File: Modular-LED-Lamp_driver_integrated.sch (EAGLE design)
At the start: 15 parts

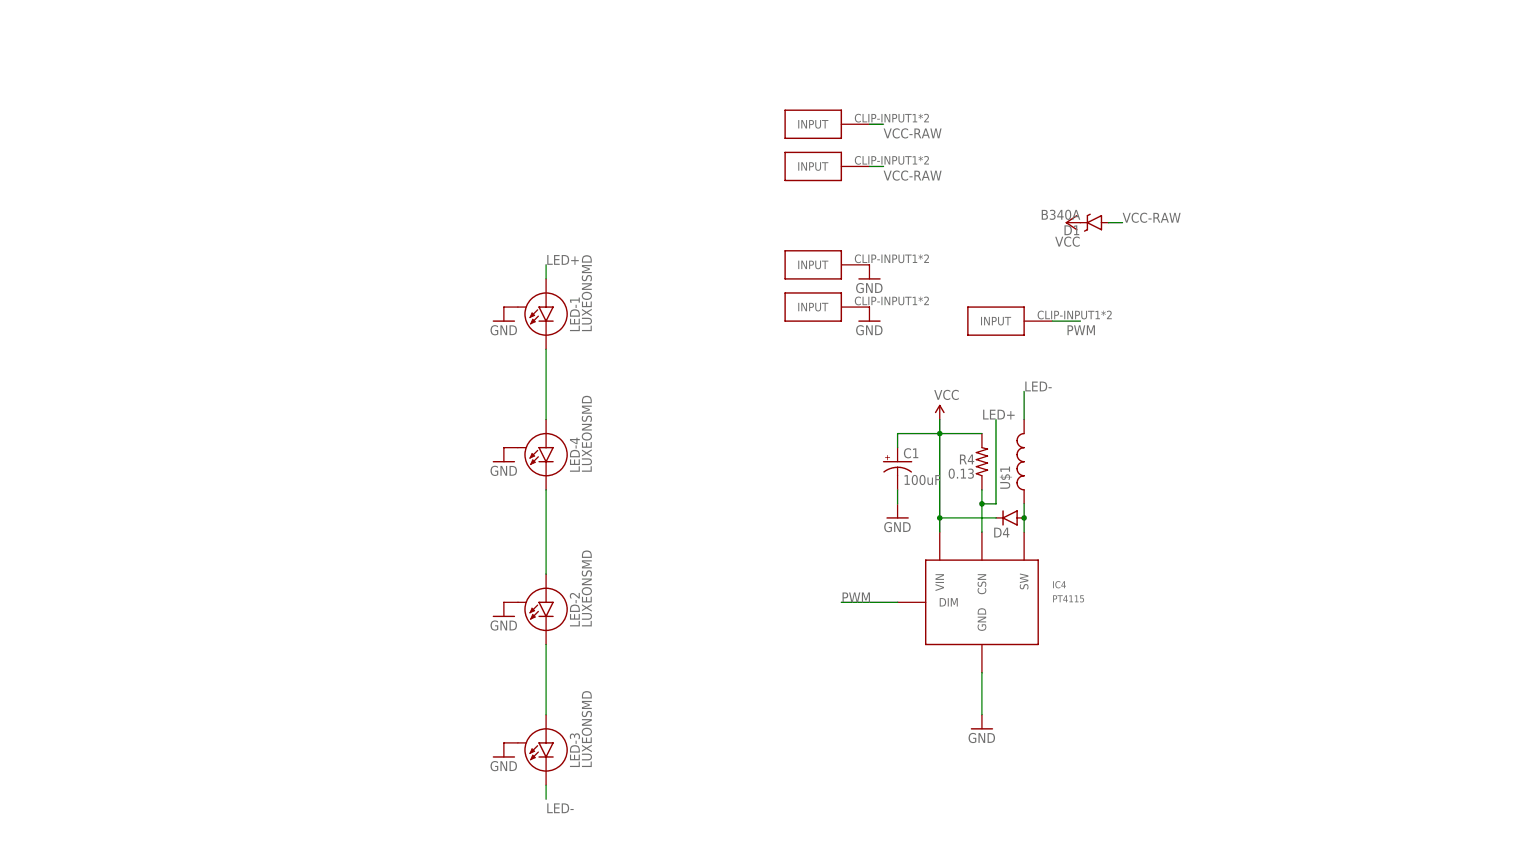
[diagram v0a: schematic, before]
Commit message: changed outline to be bigger to disspate more heat, added footprint for 90° turned fuse holders, rounded edges
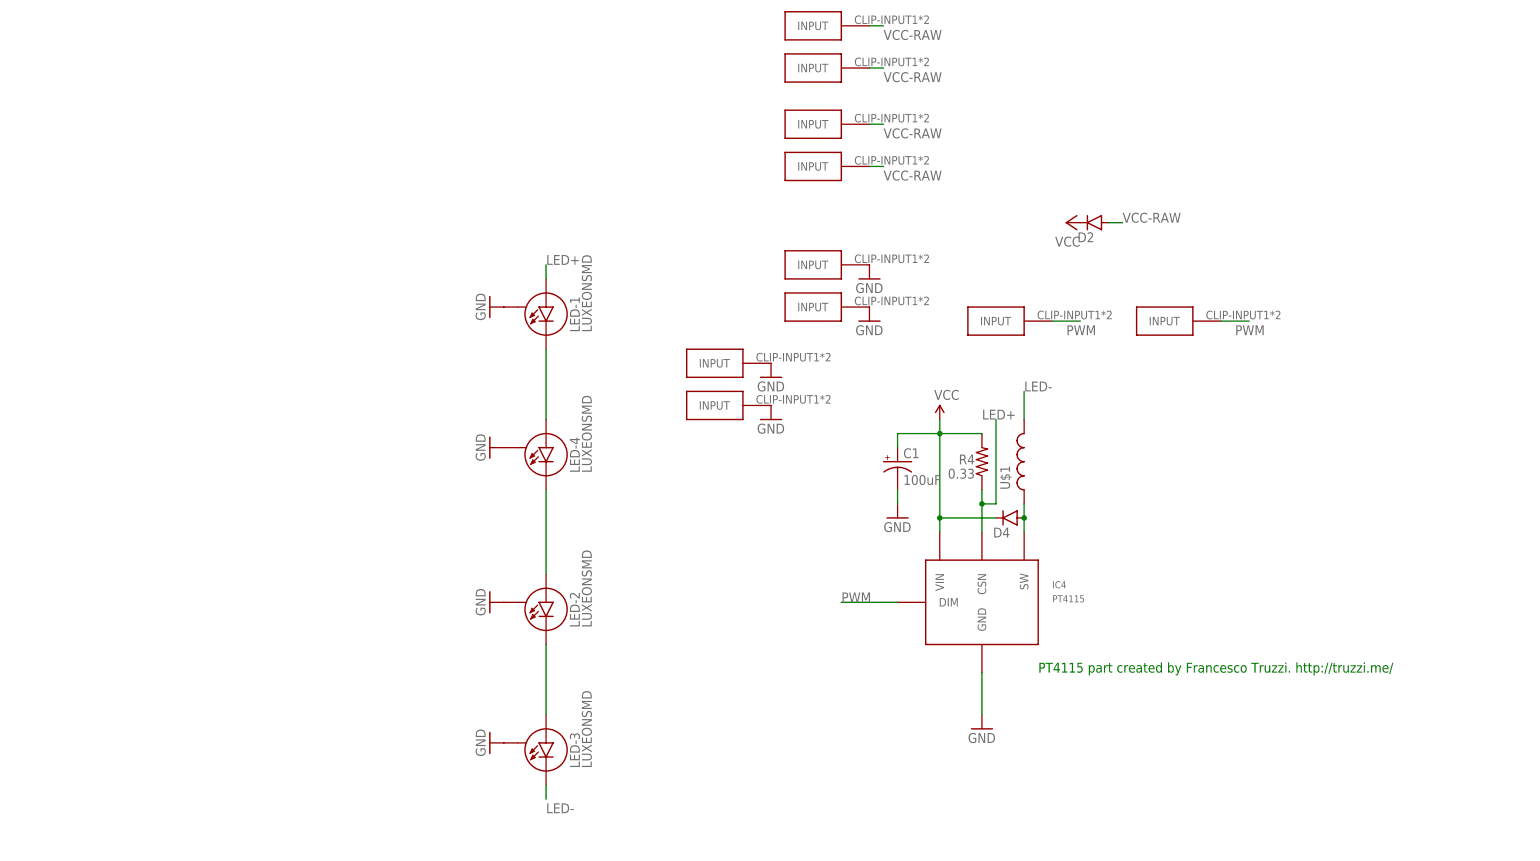
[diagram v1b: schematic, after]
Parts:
- removed D1: B340A, SparkFun-DiscreteSemi:DIODE-SCHOTTKY-B340A
- added D2: (no value), SparkFun-DiscreteSemi:DIODESMA-KIT
- added GND-CLIP1, GND-CLIP3: GND, timon-diverses:FUSE-HOLDER-5X20MM
- added PWM-CLIP1, VCC-CLIP1, VCC-CLIP3: FUSE-HOLDER-5X20MM, timon-diverses:FUSE-HOLDER-5X20MM
- R4: value 0.13 -> 0.33
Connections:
- net GND: now also GND-CLIP1.INPUT, GND-CLIP3.INPUT
- net PWM: now also PWM-CLIP1.INPUT
- net VCC: now also D2.C; no longer D1.C
- net VCC-RAW: now also D2.A, VCC-CLIP1.INPUT, VCC-CLIP3.INPUT; no longer D1.A
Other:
- note added: "PT4115 part created by Francesco Truzzi. http://truzzi.me/"
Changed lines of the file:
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@@
 <part name="SUPPLY4" library="SparkFun-Aesthetics" deviceset="VCC" device=""/>
 <part name="GND8" library="SparkFun-Aesthetics" deviceset="GND" device=""/>
-<part name="R4" library="SparkFun-Resistors" deviceset="0.3OHM-1/8W-1%(0805)" device="" value="0.13"/>
+<part name="R4" library="SparkFun-Resistors" deviceset="0.3OHM-1/8W-1%(0805)" device="" value="0.33"/>
 <part name="D4" library="SparkFun-DiscreteSemi" deviceset="DIODE" device="SMA-KIT"/>
 <part name="GND9" library="SparkFun-Aesthetics" deviceset="GND" device=""/>
 <part name="C1" library="SparkFun-Capacitors" deviceset="CAP_POL" device="E" value="100uF"/>
-<part name="D1" library="SparkFun-DiscreteSemi" deviceset="DIODE-SCHOTTKY" device="-B340A" value="B340A"/>
+<part name="U$1" library="inductor-coilcraft" deviceset="MSS1260" device=""/>
 <part name="GND1" library="supply1" deviceset="GND" device=""/>
 <part name="GND2" library="supply1" deviceset="GND" device=""/>
 <part name="GND3" library="supply1" deviceset="GND" device=""/>
 <part name="GND4" library="supply1" deviceset="GND" device=""/>
-<part name="U$1" library="inductor-coilcraft" deviceset="MSS1260" device=""/>
+<part name="VCC-CLIP1" library="timon-diverses" deviceset="FUSE-HOLDER-5X20MM" device=""/>
+<part name="VCC-CLIP3" library="timon-diverses" deviceset="FUSE-HOLDER-5X20MM" device=""/>
+<part name="GND-CLIP1" library="timon-diverses" deviceset="FUSE-HOLDER-5X20MM" device="" value="GND"/>
+<part name="GND-CLIP3" library="timon-diverses" deviceset="FUSE-HOLDER-5X20MM" device="" value="GND"/>
+<part name="GND5" library="supply1" deviceset="GND" device=""/>
+<part name="GND6" library="supply1" deviceset="GND" device=""/>
+<part name="PWM-CLIP1" library="timon-diverses" deviceset="FUSE-HOLDER-5X20MM" device=""/>
+<part name="D2" library="SparkFun-DiscreteSemi" deviceset="DIODE" device="SMA-KIT"/>
 </parts>
 <sheets>
 <sheet>
 <plain>
+<text x="111.76" y="-38.1" size="1.778" layer="91">PT4115 part created by Francesco Truzzi. http://truzzi.me/</text>
 </plain>
 <instances>
@@
 <instance part="GND9" gate="1" x="86.36" y="-10.16"/>
 <instance part="C1" gate="G$1" x="86.36" y="0"/>
-<instance part="D1" gate="G$1" x="121.92" y="43.18" rot="R180"/>
-<instance part="GND1" gate="1" x="15.24" y="-27.94"/>
-<instance part="GND2" gate="1" x="15.24" y="-53.34"/>
-<instance part="GND3" gate="1" x="15.24" y="0"/>
-<instance part="GND4" gate="1" x="15.24" y="25.4"/>
 <instance part="U$1" gate="G$1" x="109.22" y="0"/>
+<instance part="GND1" gate="1" x="12.7" y="27.94" rot="R270"/>
+<instance part="GND2" gate="1" x="12.7" y="2.54" rot="R270"/>
+<instance part="GND3" gate="1" x="12.7" y="-25.4" rot="R270"/>
+<instance part="GND4" gate="1" x="12.7" y="-50.8" rot="R270"/>
+<instance part="VCC-CLIP1" gate="CLIP" x="71.12" y="78.74"/>
+<instance part="VCC-CLIP3" gate="CLIP" x="71.12" y="71.12"/>
+<instance part="GND-CLIP1" gate="CLIP" x="53.34" y="17.78"/>
+<instance part="GND-CLIP3" gate="CLIP" x="53.34" y="10.16"/>
+<instance part="GND5" gate="1" x="63.5" y="15.24"/>
+<instance part="GND6" gate="1" x="63.5" y="7.62"/>
+<instance part="PWM-CLIP1" gate="CLIP" x="134.62" y="25.4"/>
+<instance part="D2" gate="G$1" x="121.92" y="43.18" smashed="yes" rot="R180">
+<attribute name="NAME" x="121.92" y="41.4274" size="1.778" layer="95" rot="R180"/>
+<attribute name="VALUE" x="119.38" y="45.4914" size="1.778" layer="96" rot="R180"/>
+</instance>
 </instances>
 <busses>
@@
 <segment>
 <pinref part="P+1" gate="VCC" pin="VCC"/>
-<pinref part="D1" gate="G$1" pin="C"/>
+<pinref part="D2" gate="G$1" pin="C"/>
 </segment>
 </net>
@@
 </segment>
 <segment>
+<pinref part="LED-1" gate="G$1" pin="S"/>
+<pinref part="GND1" gate="1" pin="GND"/>
+</segment>
+<segment>
+<pinref part="LED-4" gate="G$1" pin="S"/>
+<pinref part="GND2" gate="1" pin="GND"/>
+</segment>
+<segment>
 <pinref part="LED-2" gate="G$1" pin="S"/>
-<pinref part="GND1" gate="1" pin="GND"/>
-</segment>
-<segment>
-<pinref part="LED-4" gate="G$1" pin="S"/>
 <pinref part="GND3" gate="1" pin="GND"/>
 </segment>
 <segment>
-<pinref part="LED-1" gate="G$1" pin="S"/>
+<pinref part="LED-3" gate="G$1" pin="S"/>
 <pinref part="GND4" gate="1" pin="GND"/>
 </segment>
 <segment>
-<pinref part="LED-3" gate="G$1" pin="S"/>
-<pinref part="GND2" gate="1" pin="GND"/>
+<pinref part="GND-CLIP1" gate="CLIP" pin="INPUT"/>
+<pinref part="GND5" gate="1" pin="GND"/>
+</segment>
+<segment>
+<pinref part="GND-CLIP3" gate="CLIP" pin="INPUT"/>
+<pinref part="GND6" gate="1" pin="GND"/>
 </segment>
 </net>
@@
 <label x="76.2" y="-25.4" size="1.778" layer="95"/>
 </segment>
+<segment>
+<pinref part="PWM-CLIP1" gate="CLIP" pin="INPUT"/>
+<wire x1="144.78" y1="25.4" x2="149.86" y2="25.4" width="0.1524" layer="91"/>
+<label x="147.32" y="22.86" size="1.778" layer="95"/>
+</segment>
 </net>
 <net name="N$1" class="0">
@@
 <net name="VCC-RAW" class="0">
 <segment>
-<pinref part="D1" gate="G$1" pin="A"/>
 <wire x1="124.46" y1="43.18" x2="127" y2="43.18" width="0.1524" layer="91"/>
 <label x="127" y="43.18" size="1.778" layer="95"/>
+<pinref part="D2" gate="G$1" pin="A"/>
 </segment>
 <segment>
@@
 <pinref part="VCC-CLIP2" gate="CLIP" pin="INPUT"/>
 </segment>
-</net>
+<segment>
+<wire x1="81.28" y1="78.74" x2="83.82" y2="78.74" width="0.1524" layer="91"/>
+<label x="83.82" y="76.2" size="1.778" layer="95"/>
+<pinref part="VCC-CLIP1" gate="CLIP" pin="INPUT"/>
+</segment>
+<segment>
+<wire x1="81.28" y1="71.12" x2="83.82" y2="71.12" width="0.1524" layer="91"/>
+<label x="83.82" y="68.58" size="1.778" layer="95"/>
+<pinref part="VCC-CLIP3" gate="CLIP" pin="INPUT"/>
+</segment>
+</net>

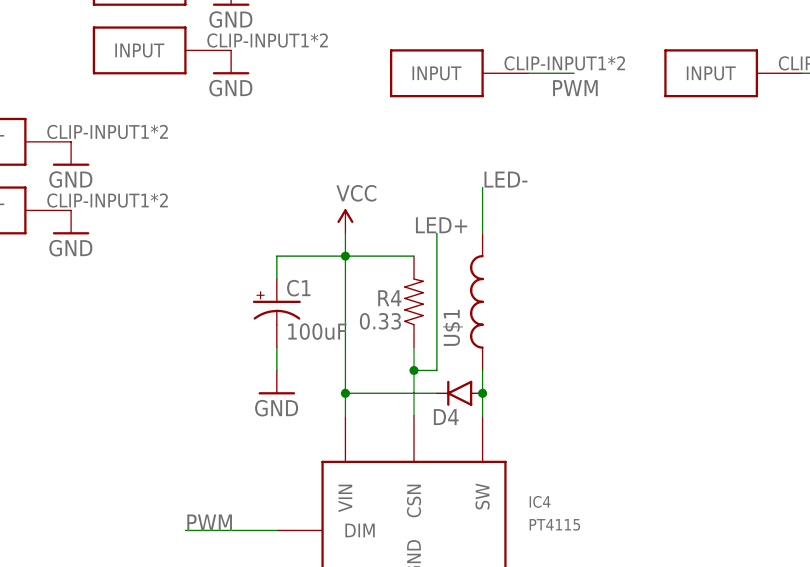
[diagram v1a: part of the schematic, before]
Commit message: updated integrated driver module to be 1W instead of 3W
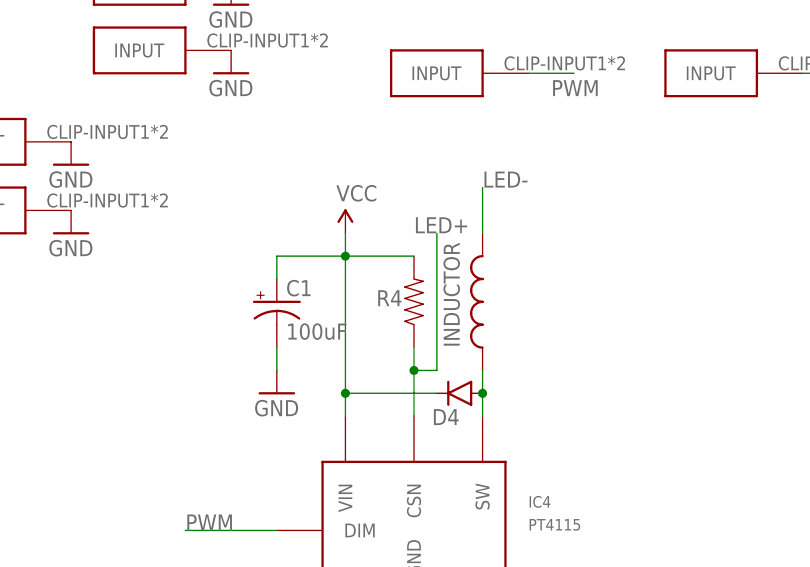
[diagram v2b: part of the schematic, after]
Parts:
- R4: value 0.33 -> 0.3; device SparkFun-Resistors:0.3OHM-1/8W-1%(0805) -> SparkFun-Resistors:RESISTOR1206
- renumbered U$1 to INDUCTOR
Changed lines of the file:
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@@
 <class number="0" name="default" width="0" drill="0">
+</class>
+<class number="1" name="VCC" width="0" drill="0">
+<clearance class="1" value="0.762"/>
 </class>
 </classes>
@@
 <part name="SUPPLY4" library="SparkFun-Aesthetics" deviceset="VCC" device=""/>
 <part name="GND8" library="SparkFun-Aesthetics" deviceset="GND" device=""/>
-<part name="R4" library="SparkFun-Resistors" deviceset="0.3OHM-1/8W-1%(0805)" device="" value="0.33"/>
+<part name="R4" library="SparkFun-Resistors" deviceset="RESISTOR" device="1206" value="0.3"/>
 <part name="D4" library="SparkFun-DiscreteSemi" deviceset="DIODE" device="SMA-KIT"/>
 <part name="GND9" library="SparkFun-Aesthetics" deviceset="GND" device=""/>
 <part name="C1" library="SparkFun-Capacitors" deviceset="CAP_POL" device="E" value="100uF"/>
-<part name="U$1" library="inductor-coilcraft" deviceset="MSS1260" device=""/>
+<part name="INDUCTOR" library="inductor-coilcraft" deviceset="MSS1260" device=""/>
 <part name="GND1" library="supply1" deviceset="GND" device=""/>
 <part name="GND2" library="supply1" deviceset="GND" device=""/>
@@
 <instance part="R4" gate="G$1" x="101.6" y="0" smashed="yes" rot="R90">
 <attribute name="NAME" x="100.33" y="1.2954" size="1.778" layer="95" rot="R180"/>
-<attribute name="VALUE" x="100.33" y="-1.27" size="1.778" layer="96" rot="R180"/>
 </instance>
 <instance part="D4" gate="G$1" x="106.68" y="-10.16" smashed="yes" rot="R180">
@@
 <instance part="GND9" gate="1" x="86.36" y="-10.16"/>
 <instance part="C1" gate="G$1" x="86.36" y="0"/>
-<instance part="U$1" gate="G$1" x="109.22" y="0"/>
+<instance part="INDUCTOR" gate="G$1" x="109.22" y="0"/>
 <instance part="GND1" gate="1" x="12.7" y="27.94" rot="R270"/>
 <instance part="GND2" gate="1" x="12.7" y="2.54" rot="R270"/>
@@
 <wire x1="109.22" y1="7.62" x2="109.22" y2="12.7" width="0.1524" layer="91"/>
 <label x="109.22" y="12.7" size="1.778" layer="95"/>
-<pinref part="U$1" gate="G$1" pin="P$1"/>
+<pinref part="INDUCTOR" gate="G$1" pin="P$1"/>
 </segment>
 </net>
@@
 <wire x1="109.22" y1="-7.62" x2="109.22" y2="-10.16" width="0.1524" layer="91"/>
 <junction x="109.22" y="-10.16"/>
-<pinref part="U$1" gate="G$1" pin="P$2"/>
-</segment>
-</net>
-<net name="VCC-RAW" class="0">
+<pinref part="INDUCTOR" gate="G$1" pin="P$2"/>
+</segment>
+</net>
+<net name="VCC-RAW" class="1">
 <segment>
 <wire x1="124.46" y1="43.18" x2="127" y2="43.18" width="0.1524" layer="91"/>

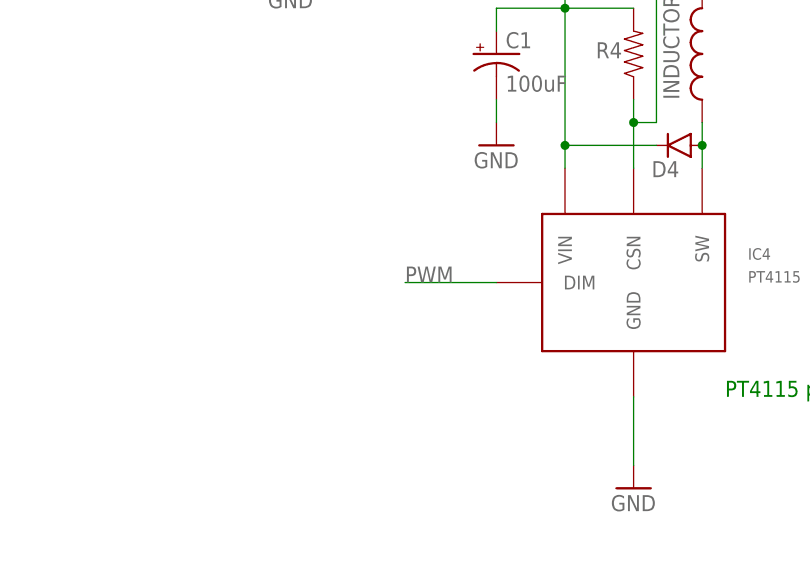
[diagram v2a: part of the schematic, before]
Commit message: fixed issued with PWM rod causing short circuit when two boards are mounted with one being reversed. Added PDF for schematic and board.
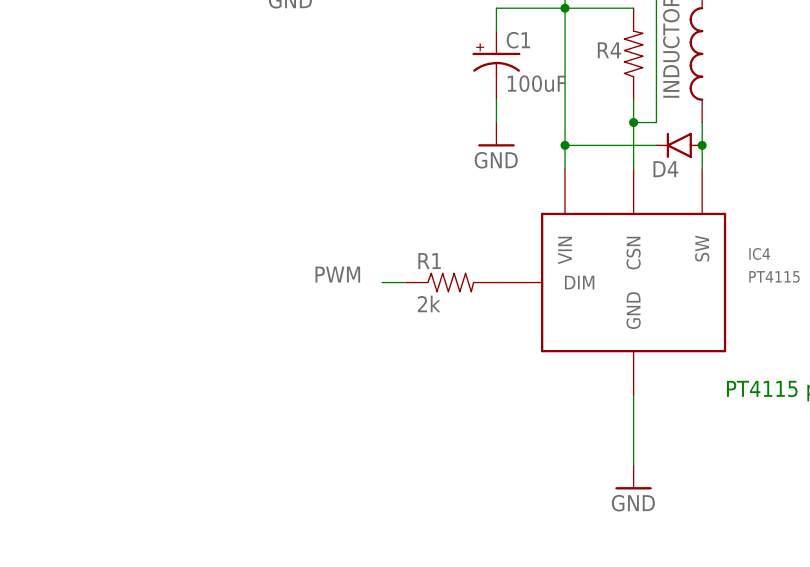
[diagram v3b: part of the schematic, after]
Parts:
- added R1: 2k, SparkFun-Resistors:RESISTOR1206
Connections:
- new net N$5: IC4.DIM, R1.2
- net PWM: now also R1.1; no longer IC4.DIM
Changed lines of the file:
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@@
 <part name="PWM-CLIP1" library="timon-diverses" deviceset="FUSE-HOLDER-5X20MM" device=""/>
 <part name="D2" library="SparkFun-DiscreteSemi" deviceset="DIODE" device="SMA-KIT"/>
+<part name="R1" library="SparkFun-Resistors" deviceset="RESISTOR" device="1206" value="2k"/>
 </parts>
 <sheets>
@@
 <attribute name="VALUE" x="119.38" y="45.4914" size="1.778" layer="96" rot="R180"/>
 </instance>
+<instance part="R1" gate="G$1" x="81.28" y="-25.4"/>
 </instances>
 <busses>
@@
 </segment>
 <segment>
-<pinref part="IC4" gate="IC" pin="DIM"/>
-<wire x1="86.36" y1="-25.4" x2="76.2" y2="-25.4" width="0.1524" layer="91"/>
-<label x="76.2" y="-25.4" size="1.778" layer="95"/>
-</segment>
-<segment>
 <pinref part="PWM-CLIP1" gate="CLIP" pin="INPUT"/>
 <wire x1="144.78" y1="25.4" x2="149.86" y2="25.4" width="0.1524" layer="91"/>
 <label x="147.32" y="22.86" size="1.778" layer="95"/>
+</segment>
+<segment>
+<pinref part="R1" gate="G$1" pin="1"/>
+<wire x1="76.2" y1="-25.4" x2="73.66" y2="-25.4" width="0.1524" layer="91"/>
+<label x="66.04" y="-25.4" size="1.778" layer="95"/>
 </segment>
 </net>
@@
 </segment>
 </net>
+<net name="N$5" class="0">
+<segment>
+<pinref part="IC4" gate="IC" pin="DIM"/>
+<pinref part="R1" gate="G$1" pin="2"/>
+</segment>
+</net>
